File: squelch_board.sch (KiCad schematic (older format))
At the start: 84 parts, among them P1 PWR, P2 DISC., P3 OUT, P4 CONN_02X04, P5 CONN-10033526-N3212LF, P6 CONN_01X05, P7 LPF, P8 HPF, P9 DISC., U1 STM32F070F6P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

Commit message: Adding note to schematic about optional input LPF
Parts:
- C25: value 470p -> NP
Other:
- note added: "Optional LPF"
- note added: "Todo:\n- output divider\n- 576-3193-1-ND LDO with smaller footprint"
- note removed: "Todo:\n- Taper off\n- output divider\n- R2\n- 576-3193-1-ND LDO with smaller footprint"
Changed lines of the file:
@@
 	1    0    0    -1
 $EndComp
-Text Notes 2225 3375 0    60   ~ 0
+Text Notes 2675 3400 0    60   ~ 0
 x 2 buffer amp
 Text Notes 4400 3400 0    60   ~ 0
@@
 Text Notes 4100 6425 0    60   ~ 0
 3rd order Butterworth Sallen-Key HPF, cutoff 7.5 kHz
-Text Notes 6125 2425 0    60   ~ 0
-Todo:\n- Taper off\n- output divider\n- R2\n- 576-3193-1-ND LDO with smaller footprint
 Text Notes 550  1050 0    300  ~ 60
 HB9UF Squelch Board Rev 2.0
@@
 ~RST
 Text Label 9050 1125 2    60   ~ 0
-BOOT0
-Text Label 10350 4150 0    60   ~ 0
 BOOT0
 Text Label 10525 3300 2    60   ~ 0
@@
 P 2025 3500
 F 0 "C25" H 1850 3450 50  0000 C CNN
-F 1 "470p" H 1800 3550 50  0000 C CNN
+F 1 "NP" H 1800 3550 50  0000 C CNN
 F 2 "Capacitor_SMD:C_0603_1608Metric" H 2063 3350 50  0001 C CNN
 F 3 "" H 2025 3500 50  0000 C CNN
@@
 NoConn ~ 10350 3600
 NoConn ~ 10350 4050
-NoConn ~ 10350 4250
 NoConn ~ 10350 4350
 NoConn ~ 10350 4450
@@
 Wire Wire Line
 	8725 3450 8950 3450
+NoConn ~ 10350 4250
+Text Label 10350 4150 0    60   ~ 0
+BOOT0
+Wire Notes Line
+	1025 3150 2350 3150
+Wire Notes Line
+	2350 3150 2350 3650
+Wire Notes Line
+	2350 3650 1025 3650
+Wire Notes Line
+	1025 3650 1025 3150
+Text Notes 1700 3275 0    60   ~ 0
+Optional LPF
+Text Notes 6125 2425 0    60   ~ 0
+Todo:\n- output divider\n- 576-3193-1-ND LDO with smaller footprint
 $EndSCHEMATC

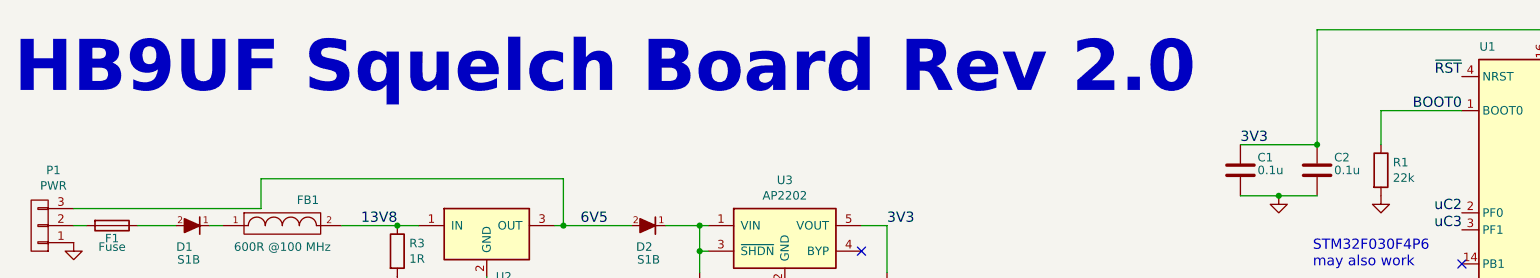
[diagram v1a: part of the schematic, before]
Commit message: Renaming "Squelch Board" to "HB9UF Smart Squelch"
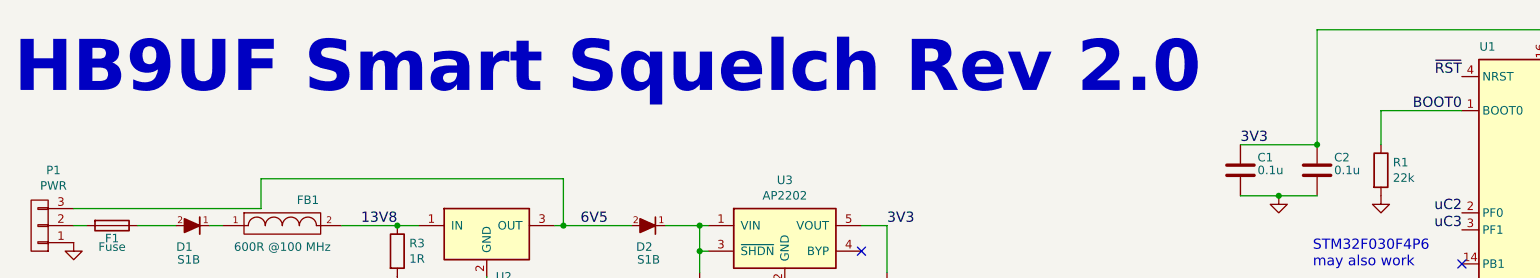
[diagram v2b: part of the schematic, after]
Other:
- note added: "HB9UF Smart Squelch Rev 2.0"
- note removed: "HB9UF Squelch Board Rev 2.0"
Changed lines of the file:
@@
 3rd order Butterworth Sallen-Key HPF, cutoff 7.5 kHz
 Text Notes 550  1050 0    300  ~ 60
-HB9UF Squelch Board Rev 2.0
+HB9UF Smart Squelch Rev 2.0
 $Comp
 L squelch_board-rescue:C C17
